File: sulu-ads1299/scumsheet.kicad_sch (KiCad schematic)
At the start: 17 parts, among them J11 through_hole, J16 through_hole, J17 through_hole, J20 through_hole, J4 through_hole, J5 through_hole, J6 through_hole, J8 through_hole, U5 scum3

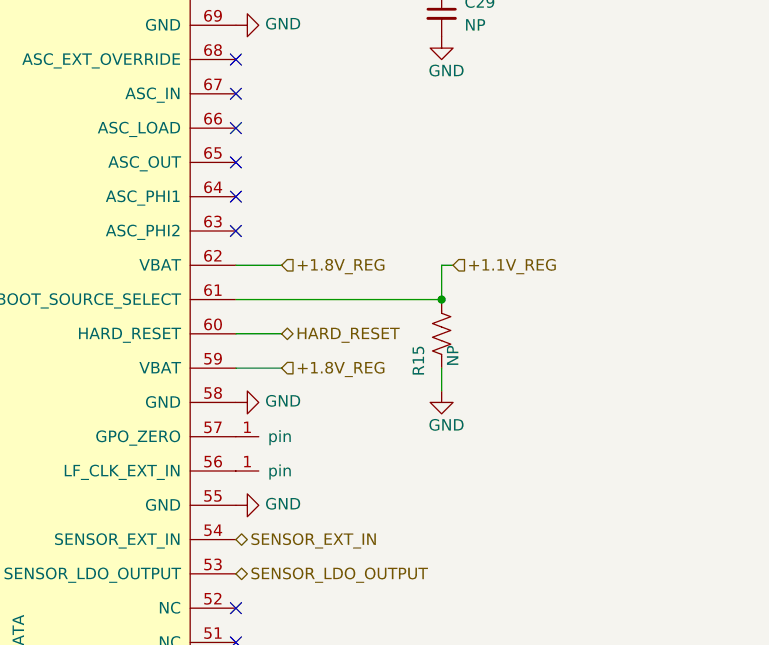
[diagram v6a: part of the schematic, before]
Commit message: Sulu-ADS1299 and connector board layout+sch progress
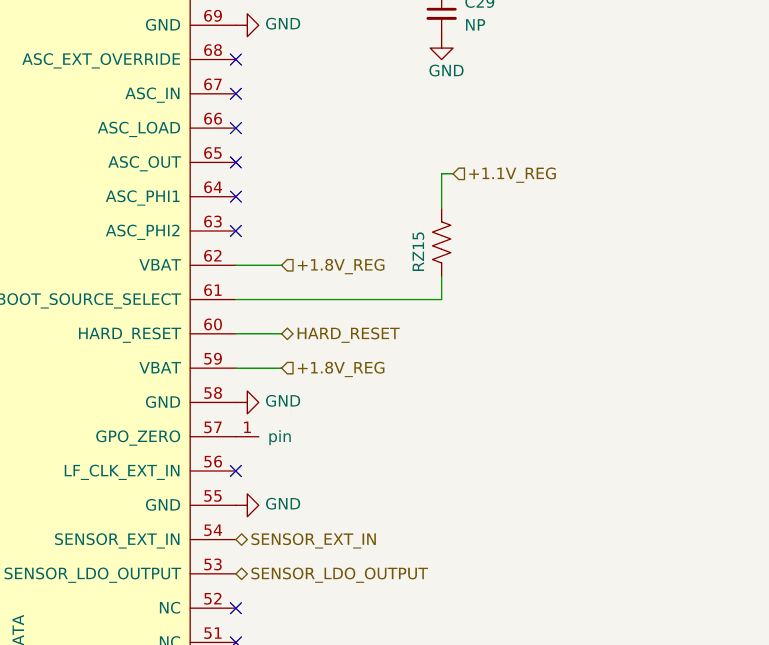
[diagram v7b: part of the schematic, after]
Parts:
- removed J17: through_hole, SCUM:through_hole, symbol draft1library:through_hole
- removed R15: NP, Resistor_SMD:R_0402_1005Metric, symbol Device:R_US
- added RZ15: (no value), symbol Device:R_US
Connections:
- net +1.1V_REG: now also RZ15.2; no longer U5.61 (BOOT_SOURCE_SELECT)
- new net: RZ15.1, U5.61 (BOOT_SOURCE_SELECT)
- no-connect marks 42 -> 43
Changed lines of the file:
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@@
   (junction (at 245.11 60.96) (diameter 0) (color 0 0 0 0)
-  )
-  (junction (at 232.41 102.87) (diameter 0) (color 0 0 0 0)
   )
   (junction (at 238.76 60.96) (diameter 0) (color 0 0 0 0)
@@
   (no_connect (at 156.21 29.21))
   (no_connect (at 171.45 29.21))
+  (no_connect (at 209.55 121.92))
   (no_connect (at 63.5 77.47))
   (no_connect (at 160.02 29.21))
@@
   (no_connect (at 144.78 29.21))
   (no_connect (at 118.11 29.21))
-  (wire (pts (xy 233.68 99.06) (xy 232.41 99.06))
-    (stroke (width 0) (type default) (color 0 0 0 0))
-  )
   (wire (pts (xy 209.55 64.77) (xy 218.44 64.77))
     (stroke (width 0) (type default) (color 0 0 0 0))
@@
     (stroke (width 0) (type default) (color 0 0 0 0))
   )
-  (wire (pts (xy 232.41 99.06) (xy 232.41 102.87))
+  (wire (pts (xy 232.41 100.33) (xy 232.41 102.87))
+    (stroke (width 0) (type default) (color 0 0 0 0))
+  )
+  (wire (pts (xy 233.68 88.9) (xy 232.41 88.9))
     (stroke (width 0) (type default) (color 0 0 0 0))
   )
@@
     (stroke (width 0) (type default) (color 0 0 0 0))
   )
-  (wire (pts (xy 232.41 110.49) (xy 232.41 113.03))
-    (stroke (width 0) (type default) (color 0 0 0 0))
-  )
   (wire (pts (xy 238.76 66.04) (xy 245.11 66.04))
     (stroke (width 0) (type default) (color 0 0 0 0))
@@
     (stroke (width 0) (type default) (color 0 0 0 0))
   )
+  (wire (pts (xy 232.41 88.9) (xy 232.41 92.71))
+    (stroke (width 0) (type default) (color 0 0 0 0))
+  )
   (wire (pts (xy 129.54 29.21) (xy 129.54 17.78))
     (stroke (width 0) (type default) (color 0 0 0 0))
@@
     (effects (font (size 1.27 1.27)) (justify left))
   )
+  (hierarchical_label "+1.1V_REG" (shape input) (at 233.68 88.9 0)
+    (effects (font (size 1.27 1.27)) (justify left))
+  )
   (hierarchical_label "GPIO4" (shape bidirectional) (at 115.57 153.67 270)
     (effects (font (size 1.27 1.27)) (justify right))
@@
     (effects (font (size 1.27 1.27)) (justify right))
   )
-  (hierarchical_label "+1.1V_REG" (shape input) (at 233.68 99.06 0)
-    (effects (font (size 1.27 1.27)) (justify left))
-  )
   (hierarchical_label "3WB_DATA" (shape bidirectional) (at 185.42 153.67 270)
     (effects (font (size 1.27 1.27)) (justify right))
@@
     )
     (pin "1")
+  )
+  (symbol (lib_id "Device:R_US") (at 232.41 96.52 180) (unit 1)
+    (in_bom yes) (on_board yes)
+    (property "Reference" "RZ15" (id 0) (at 229.87 95.25 90)
+      (effects (font (size 1.27 1.27)) (justify left))
+    )
+    (property "Value" "" (id 1) (at 236.22 93.98 90)
+      (effects (font (size 1.27 1.27)) (justify left))
+    )
+    (property "Footprint" "" (id 2) (at 231.394 96.266 90)
+      (effects (font (size 1.27 1.27)) hide)
+    )
+    (property "Datasheet" "~" (id 3) (at 232.41 96.52 0)
+      (effects (font (size 1.27 1.27)) hide)
+    )
+    (pin "1")
+    (pin "2")
   )
   (symbol (lib_id "draft1library:through_hole") (at 91.44 29.21 90) (unit 1)
@@
     (pin "99")
   )
-  (symbol (lib_id "power:GND") (at 232.41 113.03 0) (unit 1)
-    (in_bom yes) (on_board yes)
-    (property "Reference" "#PWR01" (id 0) (at 232.41 119.38 0)
-      (effects (font (size 1.27 1.27)) hide)
-    )
-    (property "Value" "GND" (id 1) (at 234.95 116.84 0)
-      (effects (font (size 1.27 1.27)) (justify right))
-    )
-    (property "Footprint" "" (id 2) (at 232.41 113.03 0)
-      (effects (font (size 1.27 1.27)) hide)
-    )
-    (property "Datasheet" "" (id 3) (at 232.41 113.03 0)
-      (effects (font (size 1.27 1.27)) hide)
-    )
-    (pin "1")
-  )
   (symbol (lib_id "power:GND") (at 209.55 72.39 90) (unit 1)
     (in_bom yes) (on_board yes)
@@
     )
     (property "Datasheet" "" (id 3) (at 121.92 26.67 0)
-      (effects (font (size 1.27 1.27)) hide)
-    )
-    (pin "1")
-  )
-  (symbol (lib_id "draft1library:through_hole") (at 209.55 121.92 0) (unit 1)
-    (in_bom yes) (on_board yes)
-    (property "Reference" "J17" (id 0) (at 209.55 116.84 0)
-      (effects (font (size 1.27 1.27)) hide)
-    )
-    (property "Value" "through_hole" (id 1) (at 209.55 119.38 0)
-      (effects (font (size 1.27 1.27)) hide)
-    )
-    (property "Footprint" "SCUM:through_hole" (id 2) (at 209.55 121.92 0)
-      (effects (font (size 1.27 1.27)) hide)
-    )
-    (property "Datasheet" "" (id 3) (at 209.55 121.92 0)
       (effects (font (size 1.27 1.27)) hide)
     )
@@
     (pin "1")
   )
-  (symbol (lib_id "Device:R_US") (at 232.41 106.68 180) (unit 1)
-    (in_bom yes) (on_board yes)
-    (property "Reference" "R15" (id 0) (at 229.87 107.95 90)
-      (effects (font (size 1.27 1.27)) (justify left))
-    )
-    (property "Value" "NP" (id 1) (at 233.68 107.95 90)
-      (effects (font (size 1.27 1.27)) (justify left))
-    )
-    (property "Footprint" "Resistor_SMD:R_0402_1005Metric" (id 2) (at 231.394 106.426 90)
-      (effects (font (size 1.27 1.27)) hide)
-    )
-    (property "Datasheet" "~" (id 3) (at 232.41 106.68 0)
-      (effects (font (size 1.27 1.27)) hide)
-    )
-    (pin "1")
-    (pin "2")
-  )
   (symbol (lib_id "draft1library:through_hole") (at 63.5 58.42 180) (unit 1)

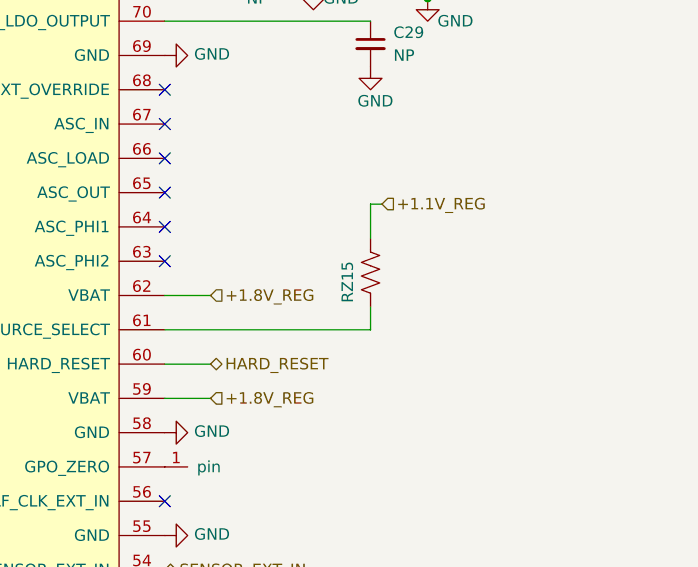
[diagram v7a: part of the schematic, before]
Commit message: Sulu-ADS1299 mosfet input protection circuit
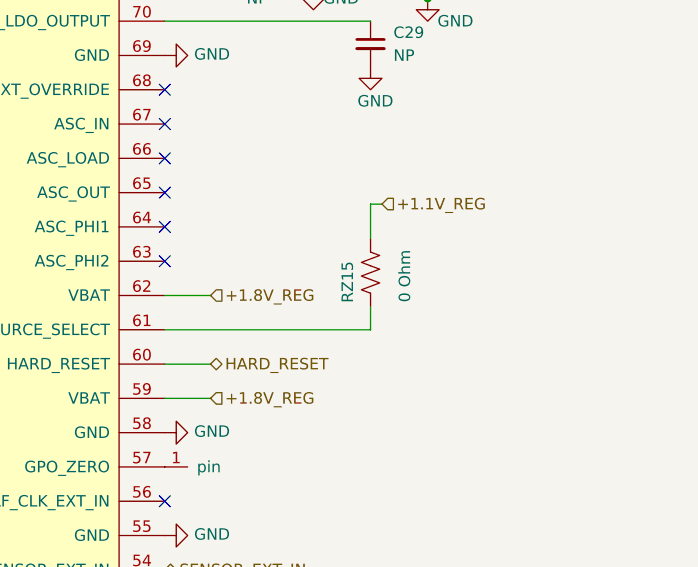
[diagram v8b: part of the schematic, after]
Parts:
- RZ15: value (none) -> 0 Ohm; footprint (none) -> Resistor_SMD:R_0402_1005Metric
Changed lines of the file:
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@@
       (effects (font (size 1.27 1.27)) (justify left))
     )
-    (property "Value" "" (id 1) (at 236.22 93.98 90)
+    (property "Value" "0 Ohm" (id 1) (at 236.22 93.98 90)
       (effects (font (size 1.27 1.27)) (justify left))
     )
-    (property "Footprint" "" (id 2) (at 231.394 96.266 90)
+    (property "Footprint" "Resistor_SMD:R_0402_1005Metric" (id 2) (at 231.394 96.266 90)
       (effects (font (size 1.27 1.27)) hide)
     )
